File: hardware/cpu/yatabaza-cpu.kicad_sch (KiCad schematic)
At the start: 28 parts, among them P1 SCREW, P10 uSD, P11 HOST, P12 KEYBOARD, P13 MIDI, P2 SCREW, P3 BUS, P4 POWER, P5 SUPPORT, P7 RTC, P8 PANEL, P9 LD, U1 STM32F103 BLUE PILL, U2 74HCT04, U3 6N138

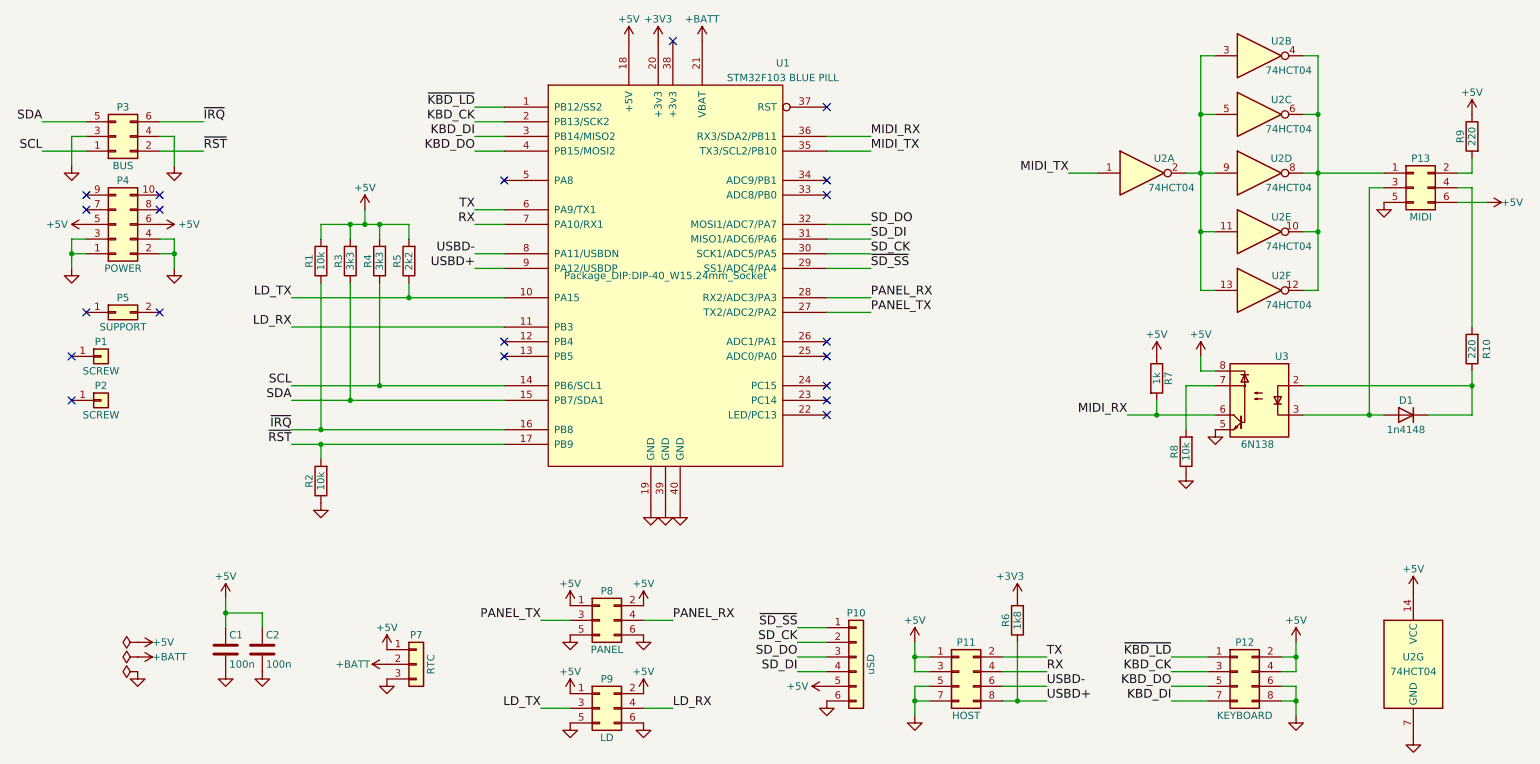
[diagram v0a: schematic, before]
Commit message: ~ Change resistors to US style.
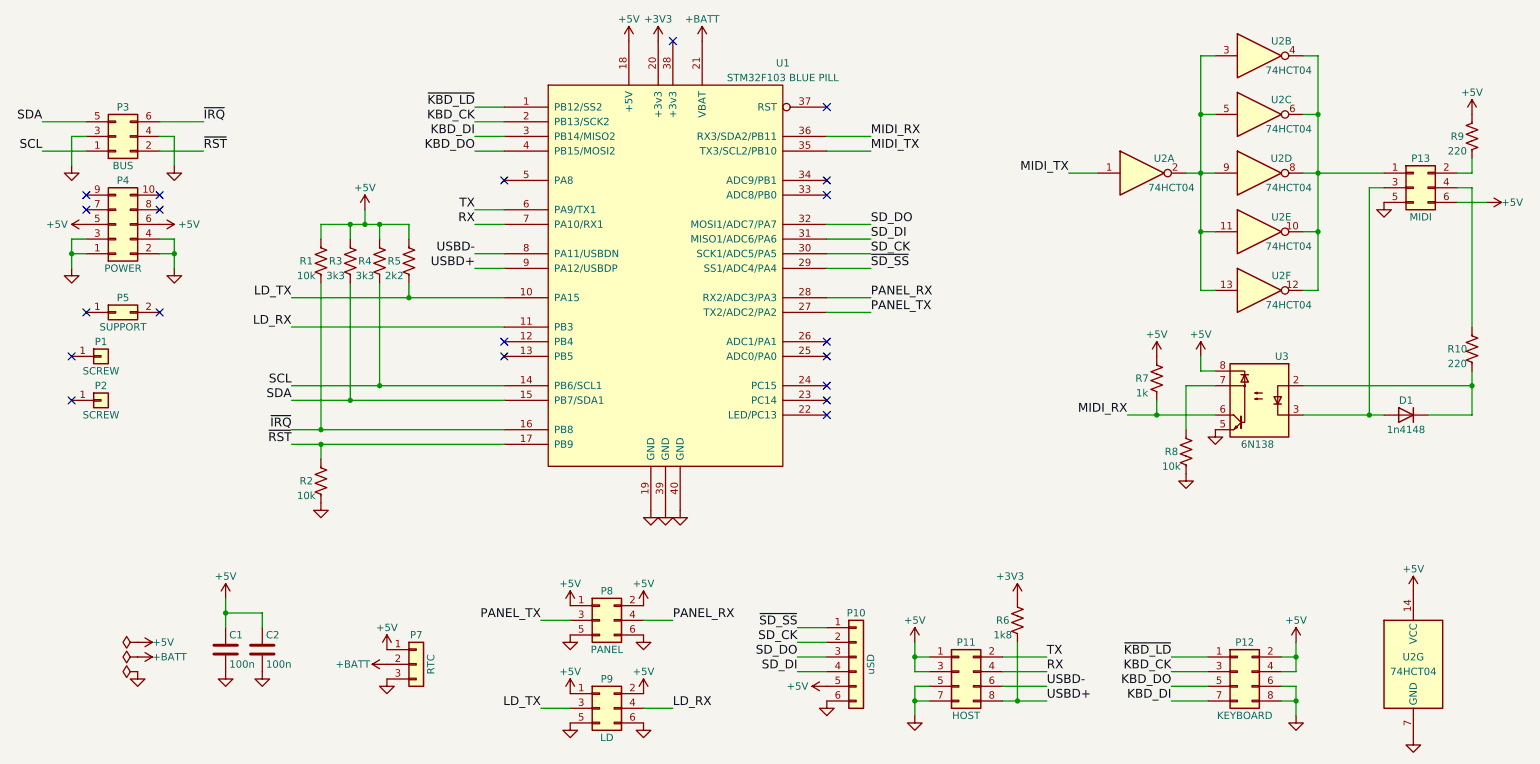
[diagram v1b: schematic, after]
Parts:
- R1, R10, R2, R3, R4, R5, R6, R7, R8, R9: symbol Device:R -> Device:R_US
- U1: footprint Package_DIP:DIP-40_W15.24mm_Socket -> (none)
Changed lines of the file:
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@@
     (pin "8")
   )
-  (symbol (lib_id "Device:R") (at 269.24 74.93 180) (unit 1)
-    (in_bom yes) (on_board yes)
-    (property "Reference" "R10" (id 0) (at 271.78 74.93 90))
-    (property "Value" "220" (id 1) (at 269.24 74.93 90))
-    (property "Footprint" "Resistor_THT:R_Axial_DIN0204_L3.6mm_D1.6mm_P2.54mm_Vertical" (id 2) (at 271.018 74.93 90)
+  (symbol (lib_id "Device:R_US") (at 269.24 74.93 180) (unit 1)
+    (in_bom yes) (on_board yes)
+    (property "Reference" "R10" (id 0) (at 266.7 74.93 0))
+    (property "Value" "220" (id 1) (at 266.7 77.47 0))
+    (property "Footprint" "Resistor_THT:R_Axial_DIN0204_L3.6mm_D1.6mm_P2.54mm_Vertical" (id 2) (at 268.224 74.676 90)
       (effects (font (size 1.27 1.27)) hide)
     )
@@
     (pin "1")
   )
-  (symbol (lib_id "Device:R") (at 214.63 80.01 0) (unit 1)
-    (in_bom yes) (on_board yes)
-    (property "Reference" "R7" (id 0) (at 216.662 80.01 90))
-    (property "Value" "1k" (id 1) (at 214.63 80.01 90))
-    (property "Footprint" "Resistor_THT:R_Axial_DIN0204_L3.6mm_D1.6mm_P7.62mm_Horizontal" (id 2) (at 212.852 80.01 90)
+  (symbol (lib_id "Device:R_US") (at 214.63 80.01 0) (unit 1)
+    (in_bom yes) (on_board yes)
+    (property "Reference" "R7" (id 0) (at 212.09 80.01 0))
+    (property "Value" "1k" (id 1) (at 212.09 82.55 0))
+    (property "Footprint" "Resistor_THT:R_Axial_DIN0204_L3.6mm_D1.6mm_P7.62mm_Horizontal" (id 2) (at 215.646 80.264 90)
       (effects (font (size 1.27 1.27)) hide)
     )
@@
     (pin "1")
   )
-  (symbol (lib_id "Device:R") (at 269.24 38.1 0) (mirror y) (unit 1)
-    (in_bom yes) (on_board yes)
-    (property "Reference" "R9" (id 0) (at 267.208 38.1 90))
-    (property "Value" "220" (id 1) (at 269.24 38.1 90))
-    (property "Footprint" "Resistor_THT:R_Axial_DIN0204_L3.6mm_D1.6mm_P2.54mm_Vertical" (id 2) (at 271.018 38.1 90)
+  (symbol (lib_id "Device:R_US") (at 269.24 38.1 0) (mirror y) (unit 1)
+    (in_bom yes) (on_board yes)
+    (property "Reference" "R9" (id 0) (at 266.7 38.1 0))
+    (property "Value" "220" (id 1) (at 266.7 40.64 0))
+    (property "Footprint" "Resistor_THT:R_Axial_DIN0204_L3.6mm_D1.6mm_P2.54mm_Vertical" (id 2) (at 268.224 38.354 90)
       (effects (font (size 1.27 1.27)) hide)
     )
@@
     (pin "1")
   )
-  (symbol (lib_id "Device:R") (at 219.71 92.71 180) (unit 1)
-    (in_bom yes) (on_board yes)
-    (property "Reference" "R8" (id 0) (at 217.678 92.71 90))
-    (property "Value" "10k" (id 1) (at 219.71 92.71 90))
-    (property "Footprint" "Resistor_THT:R_Axial_DIN0204_L3.6mm_D1.6mm_P7.62mm_Horizontal" (id 2) (at 221.488 92.71 90)
+  (symbol (lib_id "Device:R_US") (at 219.71 92.71 180) (unit 1)
+    (in_bom yes) (on_board yes)
+    (property "Reference" "R8" (id 0) (at 217.17 92.71 0))
+    (property "Value" "10k" (id 1) (at 217.17 95.25 0))
+    (property "Footprint" "Resistor_THT:R_Axial_DIN0204_L3.6mm_D1.6mm_P7.62mm_Horizontal" (id 2) (at 218.694 92.456 90)
       (effects (font (size 1.27 1.27)) hide)
     )
@@
     (pin "1")
   )
-  (symbol (lib_id "Device:R") (at 190.5 121.92 180) (unit 1)
-    (in_bom yes) (on_board yes)
-    (property "Reference" "R6" (id 0) (at 188.468 121.92 90))
-    (property "Value" "1k8" (id 1) (at 190.5 121.92 90))
-    (property "Footprint" "Resistor_THT:R_Axial_DIN0204_L3.6mm_D1.6mm_P7.62mm_Horizontal" (id 2) (at 192.278 121.92 90)
+  (symbol (lib_id "Device:R_US") (at 190.5 121.92 180) (unit 1)
+    (in_bom yes) (on_board yes)
+    (property "Reference" "R6" (id 0) (at 187.96 121.92 0))
+    (property "Value" "1k8" (id 1) (at 187.96 124.46 0))
+    (property "Footprint" "Resistor_THT:R_Axial_DIN0204_L3.6mm_D1.6mm_P7.62mm_Horizontal" (id 2) (at 189.484 121.666 90)
       (effects (font (size 1.27 1.27)) hide)
     )
@@
     (pin "3")
   )
-  (symbol (lib_id "Device:R") (at 69.85 97.79 180) (unit 1)
-    (in_bom yes) (on_board yes)
-    (property "Reference" "R2" (id 0) (at 67.818 97.79 90))
-    (property "Value" "10k" (id 1) (at 69.85 97.79 90))
-    (property "Footprint" "Resistor_THT:R_Axial_DIN0204_L3.6mm_D1.6mm_P7.62mm_Horizontal" (id 2) (at 71.628 97.79 90)
+  (symbol (lib_id "Device:R_US") (at 69.85 97.79 180) (unit 1)
+    (in_bom yes) (on_board yes)
+    (property "Reference" "R2" (id 0) (at 67.31 97.79 0))
+    (property "Value" "10k" (id 1) (at 67.31 100.33 0))
+    (property "Footprint" "Resistor_THT:R_Axial_DIN0204_L3.6mm_D1.6mm_P7.62mm_Horizontal" (id 2) (at 68.834 97.536 90)
       (effects (font (size 1.27 1.27)) hide)
     )
@@
     (pin "1")
   )
-  (symbol (lib_id "Device:R") (at 69.85 59.69 180) (unit 1)
-    (in_bom yes) (on_board yes)
-    (property "Reference" "R1" (id 0) (at 67.818 59.69 90))
-    (property "Value" "10k" (id 1) (at 69.85 59.69 90))
-    (property "Footprint" "Resistor_THT:R_Axial_DIN0204_L3.6mm_D1.6mm_P7.62mm_Horizontal" (id 2) (at 71.628 59.69 90)
+  (symbol (lib_id "Device:R_US") (at 69.85 59.69 180) (unit 1)
+    (in_bom yes) (on_board yes)
+    (property "Reference" "R1" (id 0) (at 67.31 59.69 0))
+    (property "Value" "10k" (id 1) (at 67.31 62.23 0))
+    (property "Footprint" "Resistor_THT:R_Axial_DIN0204_L3.6mm_D1.6mm_P7.62mm_Horizontal" (id 2) (at 68.834 59.436 90)
       (effects (font (size 1.27 1.27)) hide)
     )
@@
     (pin "2")
   )
-  (symbol (lib_id "Device:R") (at 74.93 59.69 180) (unit 1)
-    (in_bom yes) (on_board yes)
-    (property "Reference" "R3" (id 0) (at 72.898 59.69 90))
-    (property "Value" "3k3" (id 1) (at 74.93 59.69 90))
-    (property "Footprint" "Resistor_THT:R_Axial_DIN0204_L3.6mm_D1.6mm_P7.62mm_Horizontal" (id 2) (at 76.708 59.69 90)
+  (symbol (lib_id "Device:R_US") (at 74.93 59.69 180) (unit 1)
+    (in_bom yes) (on_board yes)
+    (property "Reference" "R3" (id 0) (at 72.39 59.69 0))
+    (property "Value" "3k3" (id 1) (at 72.39 62.23 0))
+    (property "Footprint" "Resistor_THT:R_Axial_DIN0204_L3.6mm_D1.6mm_P7.62mm_Horizontal" (id 2) (at 73.914 59.436 90)
       (effects (font (size 1.27 1.27)) hide)
     )
@@
     (pin "1")
   )
-  (symbol (lib_id "Device:R") (at 80.01 59.69 180) (unit 1)
-    (in_bom yes) (on_board yes)
-    (property "Reference" "R4" (id 0) (at 77.978 59.69 90))
-    (property "Value" "3k3" (id 1) (at 80.01 59.69 90))
-    (property "Footprint" "Resistor_THT:R_Axial_DIN0204_L3.6mm_D1.6mm_P7.62mm_Horizontal" (id 2) (at 81.788 59.69 90)
+  (symbol (lib_id "Device:R_US") (at 80.01 59.69 180) (unit 1)
+    (in_bom yes) (on_board yes)
+    (property "Reference" "R4" (id 0) (at 77.47 59.69 0))
+    (property "Value" "3k3" (id 1) (at 77.47 62.23 0))
+    (property "Footprint" "Resistor_THT:R_Axial_DIN0204_L3.6mm_D1.6mm_P7.62mm_Horizontal" (id 2) (at 78.994 59.436 90)
       (effects (font (size 1.27 1.27)) hide)
     )
@@
     (property "Reference" "U1" (id 0) (at 149.86 25.4 0))
     (property "Value" "STM32F103 BLUE PILL" (id 1) (at 149.86 27.94 0))
-    (property "Footprint" "Package_DIP:DIP-40_W15.24mm_Socket" (id 2) (at 129.54 62.23 0))
+    (property "Footprint" "" (id 2) (at 129.54 62.23 0)
+      (effects (font (size 1.27 1.27)) hide)
+    )
     (property "Datasheet" "~" (id 3) (at 129.54 62.23 0))
     (pin "1")
@@
     (pin "9")
   )
-  (symbol (lib_id "Device:R") (at 85.09 59.69 180) (unit 1)
-    (in_bom yes) (on_board yes)
-    (property "Reference" "R5" (id 0) (at 83.058 59.69 90))
-    (property "Value" "2k2" (id 1) (at 85.09 59.69 90))
-    (property "Footprint" "Resistor_THT:R_Axial_DIN0204_L3.6mm_D1.6mm_P2.54mm_Vertical" (id 2) (at 86.868 59.69 90)
-      (effects (font (size 1.27 1.27)) hide)
-    )
+  (symbol (lib_id "Device:R_US") (at 85.09 59.69 180) (unit 1)
+    (in_bom yes) (on_board yes)
+    (property "Reference" "R5" (id 0) (at 82.55 59.69 0))
+    (property "Value" "2k2" (id 1) (at 82.55 62.23 0))
+    (property "Footprint" "Resistor_THT:R_Axial_DIN0204_L3.6mm_D1.6mm_P2.54mm_Vertical" (id 2) (at 84.074 59.436 90)
+      (effects (font (size 1.27 1.27)) hide)
+    )
